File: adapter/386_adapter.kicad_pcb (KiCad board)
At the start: 2 copper layers, 38.1 x 38.1 mm, 2 parts

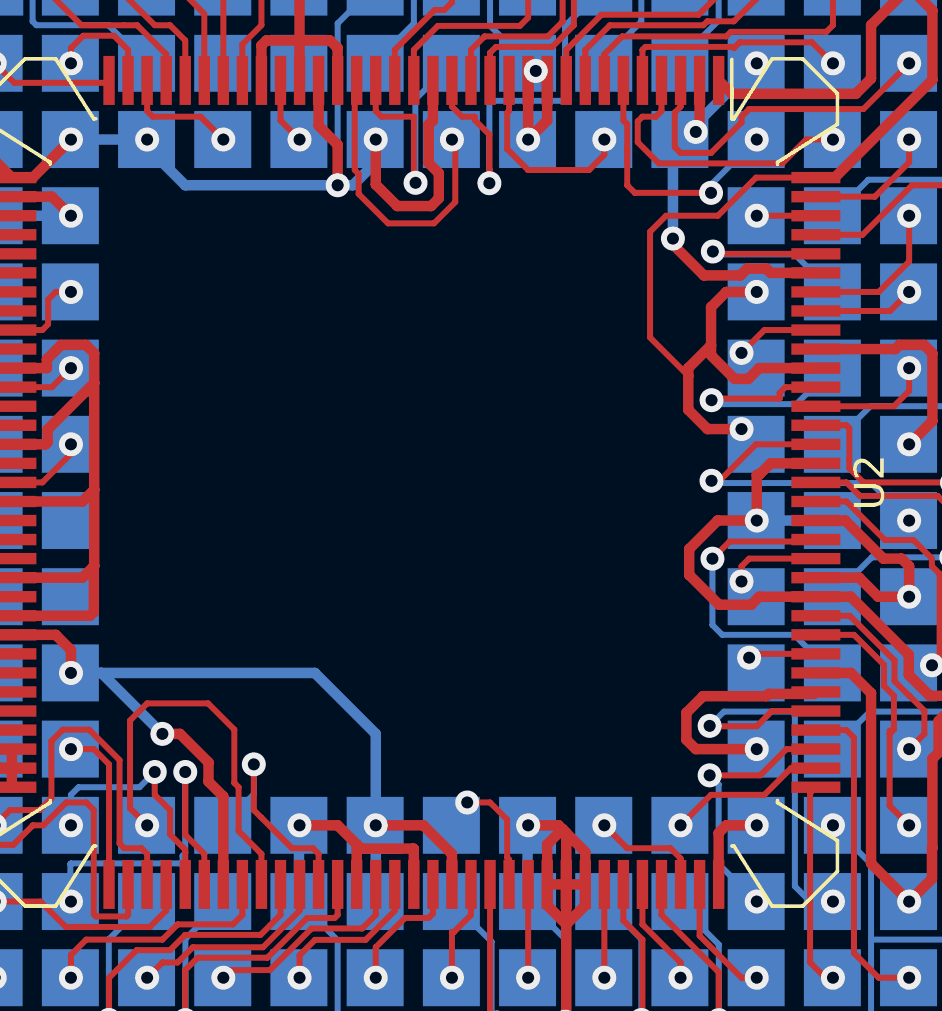
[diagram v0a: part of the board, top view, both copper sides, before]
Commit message: Add filter caps
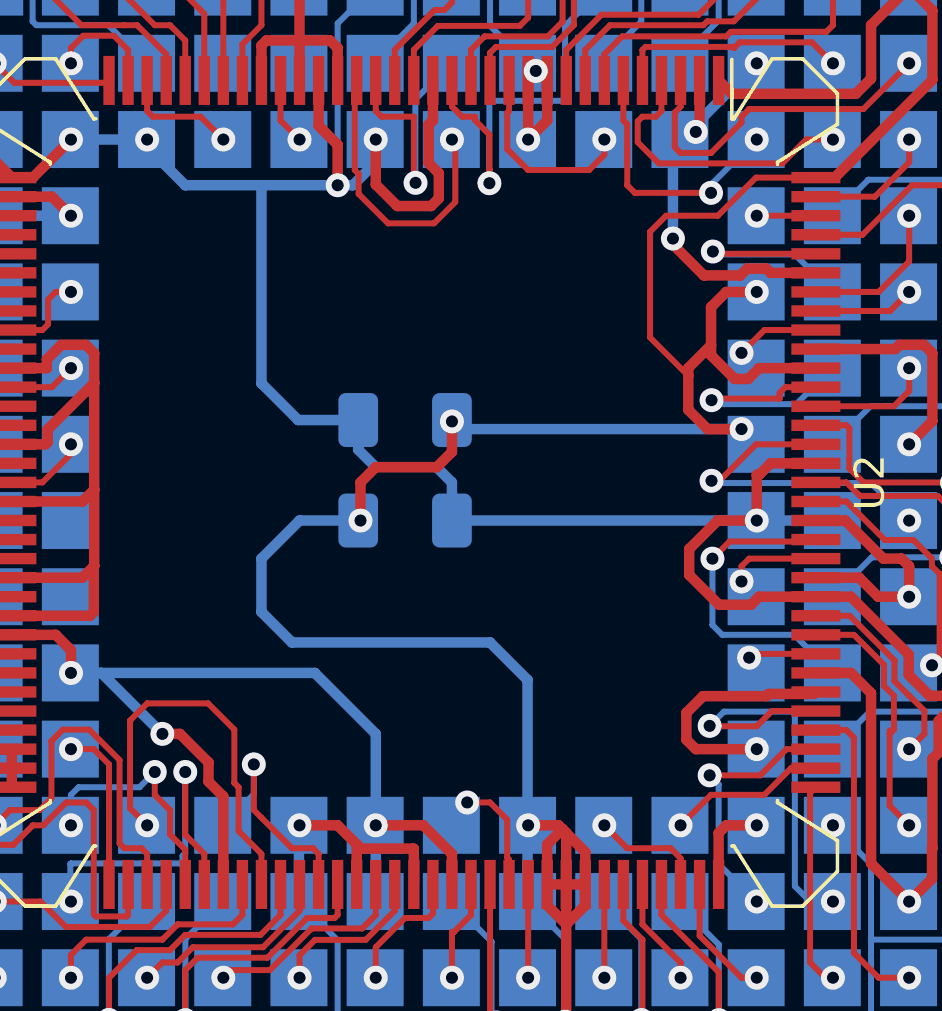
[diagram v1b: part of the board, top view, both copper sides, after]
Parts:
- added C1: 100nF, Capacitor_SMD:C_1206_3216Metric_Pad1.33x1.80mm_HandSolder, B.Cu at (114.0, 61.4)
- added C2: 100nF, Capacitor_SMD:C_1206_3216Metric_Pad1.33x1.80mm_HandSolder, B.Cu at (114.0, 64.8)
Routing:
- net GND: track 212.4 -> 248.3 mm, vias 23 -> 25
- net VCC: track 188.4 -> 214.7 mm

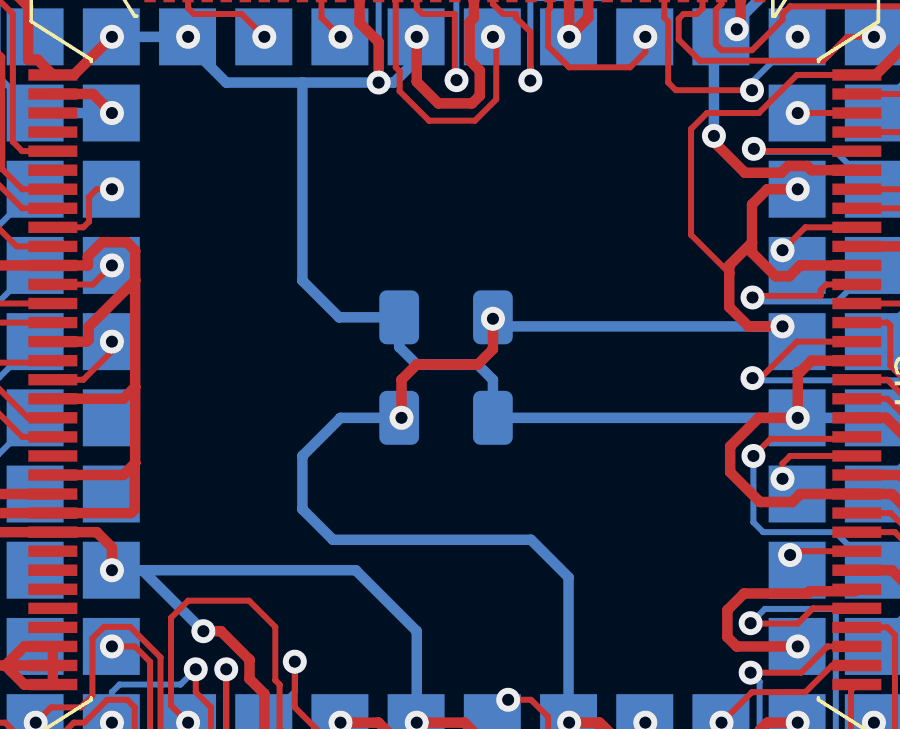
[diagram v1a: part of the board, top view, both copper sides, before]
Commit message: Added silkscreen
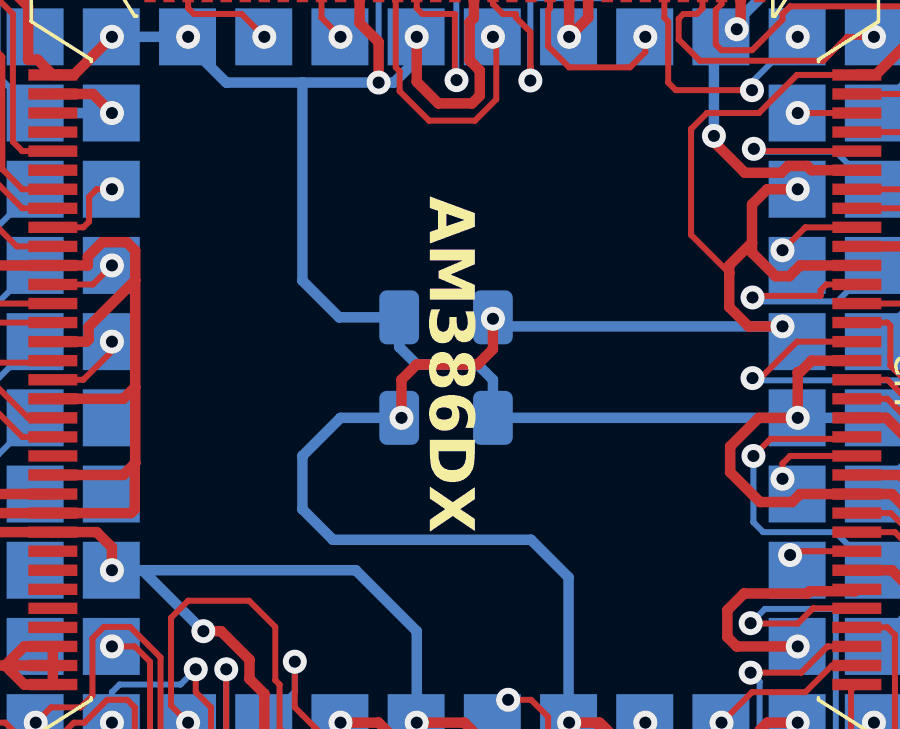
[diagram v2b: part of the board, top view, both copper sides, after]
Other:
- board text added: "AM386DX"
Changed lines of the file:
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@@
   (gr_line (start 95.25 44.45) (end 133.35 44.45)
     (stroke (width 0.1) (type default)) (layer "Edge.Cuts"))
+  (gr_text "AM386DX" (at 113.284 62.992 -90) (layer "F.SilkS")
+    (effects (font (size 1.5 1.5) (thickness 0.3) bold) (justify bottom))
+  )
   (segment (start 125.543016 67.577) (end 124.473 67.577) (width 0.35) (layer "F.Cu") (net 1))
   (segment (start 111.125 51.608984) (end 111.76 52.243984) (width 0.35) (layer "F.Cu") (net 1))

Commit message: Update PCB
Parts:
- removed C1, C2: 100nF, Capacitor_SMD:C_1206_3216Metric_Pad1.33x1.80mm_HandSolder
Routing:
- net GND: track 248.3 -> 212.4 mm, vias 25 -> 23
- net VCC: track 214.7 -> 188.4 mm
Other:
- board text removed: "AM386DX"

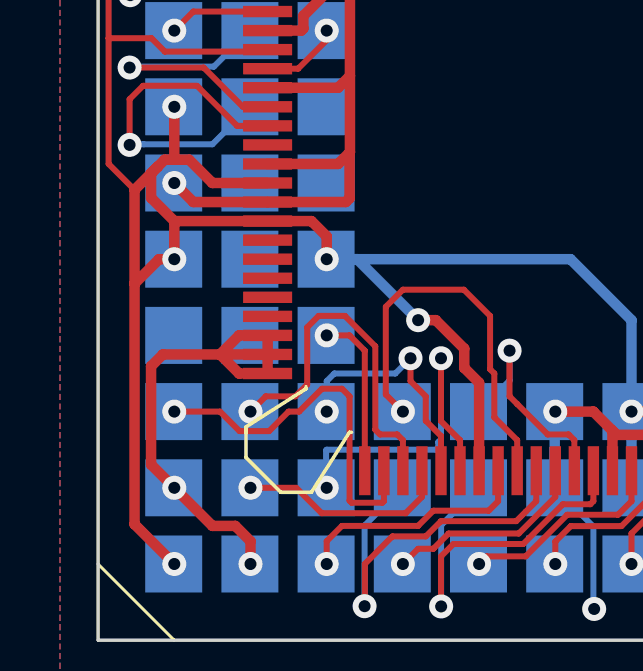
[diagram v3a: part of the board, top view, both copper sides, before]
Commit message: Updated project, plus link a GND pad that was previously left without trace
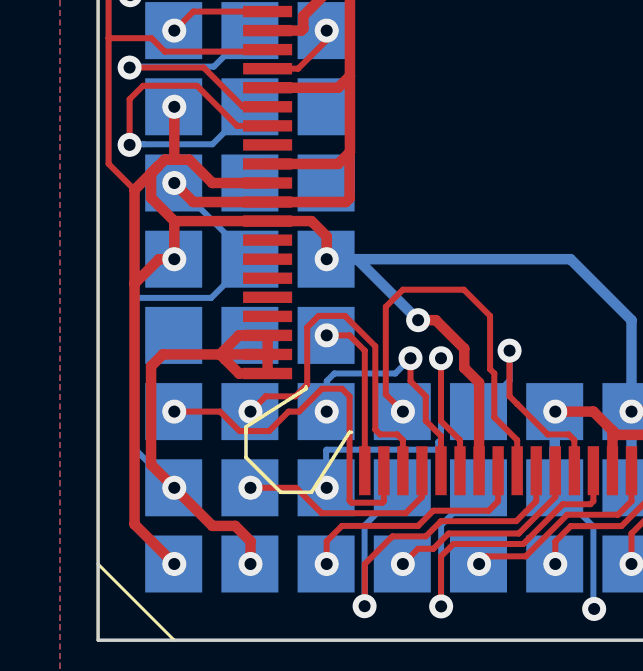
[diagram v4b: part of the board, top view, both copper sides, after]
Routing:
- net GND: track 212.4 -> 227.2 mm

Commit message: Update the project and silkscreen
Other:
- board text added: "386DX"
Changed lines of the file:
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@@
 		(layer "Edge.Cuts")
+	)
+	(gr_text "386DX"
+		(at 113.221 63.5 270)
+		(layer "F.SilkS")
+		(effects
+			(font
+				(size 2.5 2.5)
+				(thickness 0.3)
+			)
+		)
 	)
 	(segment

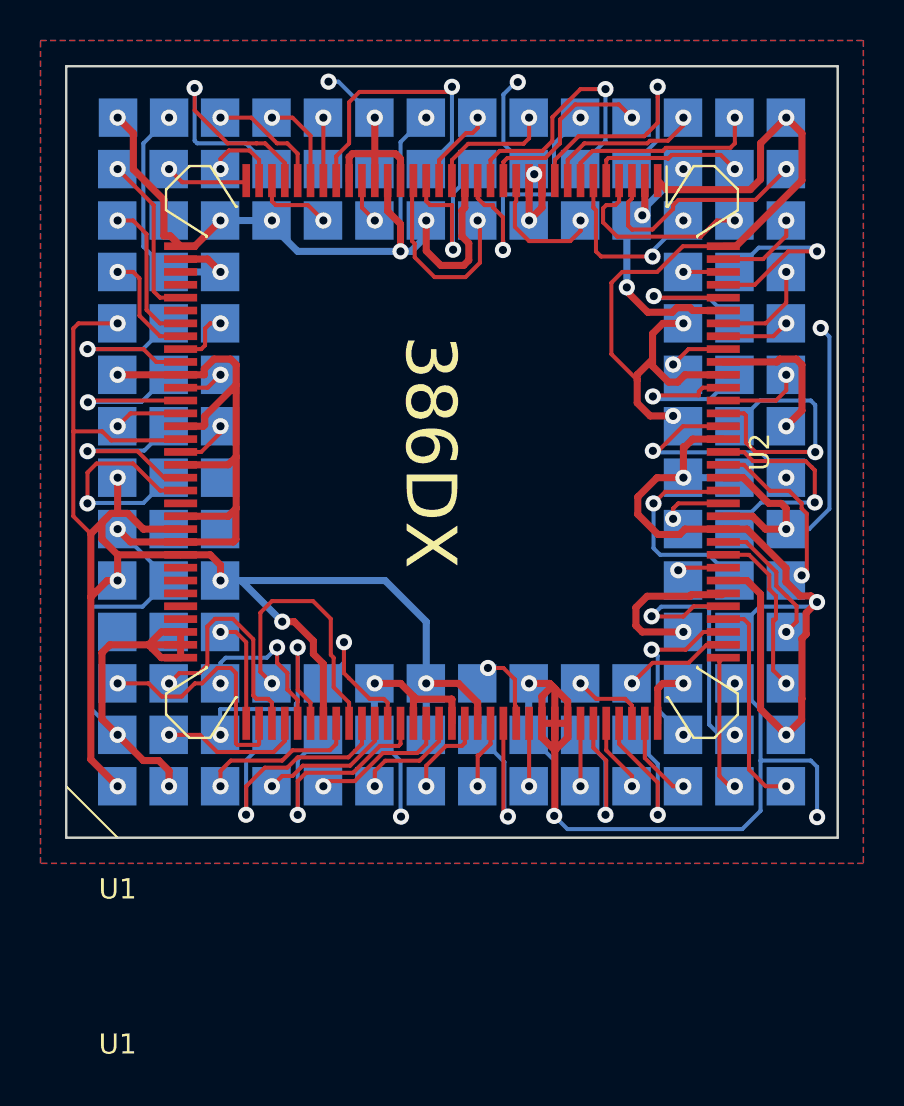
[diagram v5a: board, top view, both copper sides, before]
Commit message: Update adapter for rev.3
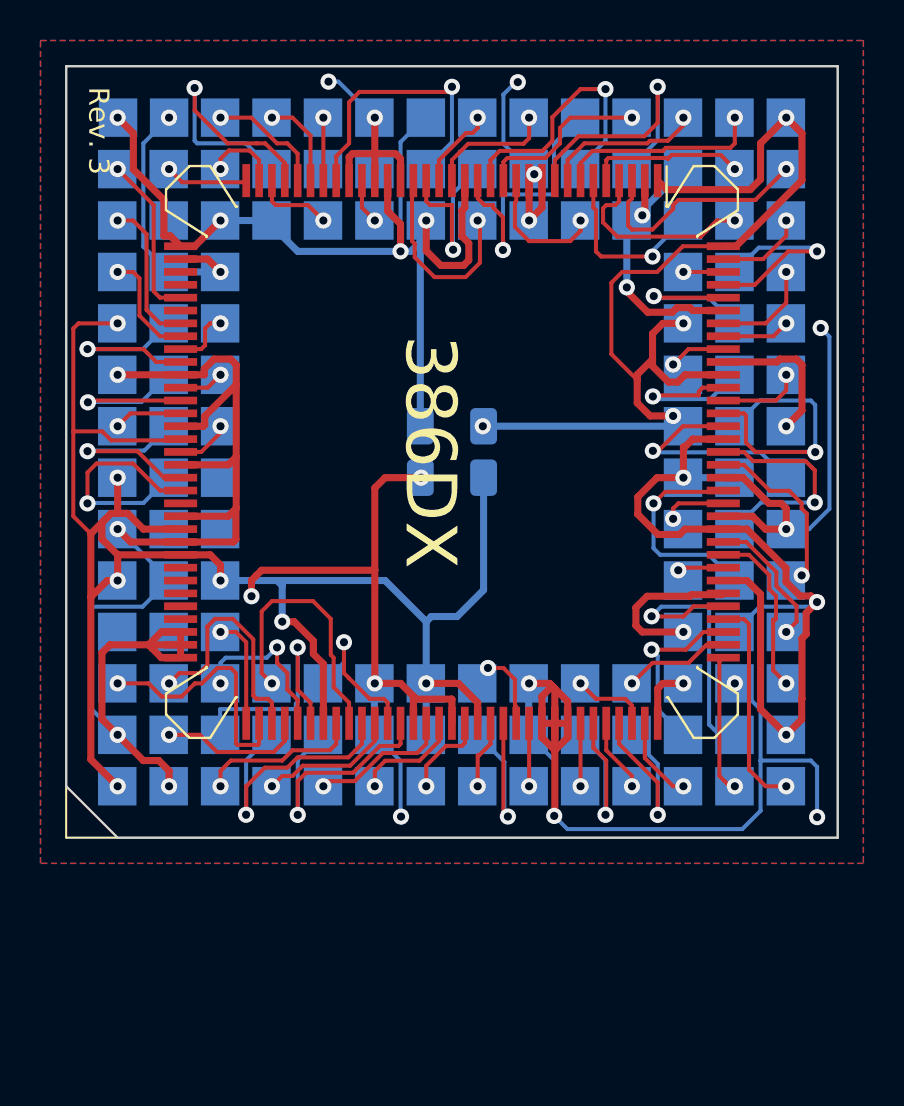
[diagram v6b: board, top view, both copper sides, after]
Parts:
- added C1: 100nF, Capacitor_SMD:C_1206_3216Metric_Pad1.33x1.80mm_HandSolder, B.Cu at (114.3, 62.2)
- added C2: 100nF, Capacitor_SMD:C_1206_3216Metric_Pad1.33x1.80mm_HandSolder, B.Cu at (114.3, 64.8)
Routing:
- net GND: track 227.2 -> 256.3 mm, vias 23 -> 26
- net VCC: track 188.4 -> 205.9 mm, vias 21 -> 18
- net /C048: track 9.40 -> 8.62 mm
- net /C052: track 9.38 -> 8.85 mm, vias 2 -> 1
- net /C066: vias 2 -> 1
- net /C046: vias 2 -> 1
- net /C030: vias 2 -> 1
- net /C028: vias 2 -> 1
- net /C006: vias 2 -> 1
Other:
- outline, holes or cut-outs redrawn
- board text added: "Rev. 3"

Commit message: Some more changes for rev.3
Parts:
- U2: footprint Package_QFP:PQFP-132_24x24mm_P0.635mm_i386 -> Custom_QFP:PQFP-132_24x24mm_P0.635mm_i386
